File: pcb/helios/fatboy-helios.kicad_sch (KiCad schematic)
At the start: 76 parts, among them SW1 SW_Push, U1 Helios

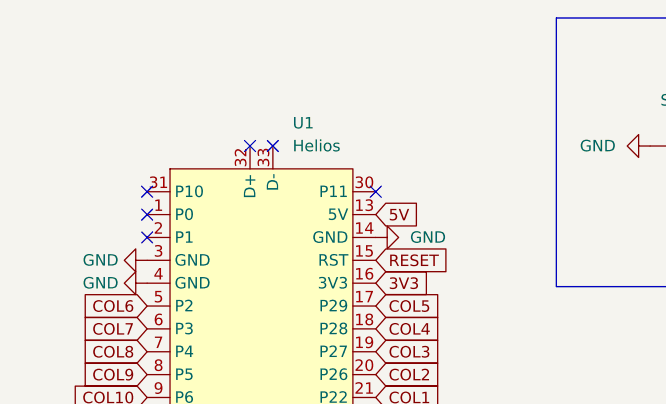
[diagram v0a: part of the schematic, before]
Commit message: helios: use `libs/marbastlib` for symbols and footprints
Instead of implicitly relying on the assumption that the `marbastlib`
(or any other library, really) will be present in development
environment, expliciltly rely on the respective submodule version
of the library
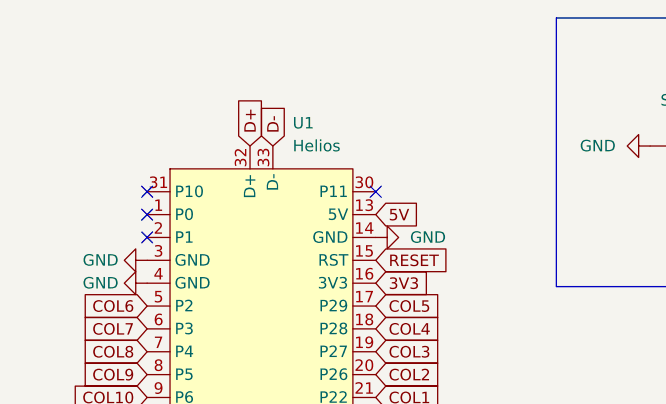
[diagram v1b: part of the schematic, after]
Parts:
- removed MX10, MX11, MX12, MX13, MX14, MX15, MX16, MX17, MX18, MX19, MX2, MX20, MX21, MX22, MX23, MX24, MX25, MX26, MX27, MX28, MX29, MX3, MX30, MX31, MX32, MX33, MX34, MX35, MX36, MX4, MX5, MX6, MX7, MX8, MX9: MX_SW_HS, PCM_marbastlib-mx:SW_MX_HS_CPG151101S11_1u, symbol PCM_marbastlib-mx:MX_SW_HS_CPG151101S11
- added MX10, MX11, MX12, MX13, MX14, MX15, MX16, MX17, MX18, MX19, MX2, MX20, MX21, MX22, MX23, MX24, MX25, MX26, MX27, MX28, MX29, MX3, MX30, MX31, MX32, MX33, MX34, MX35, MX36, MX4, MX5, MX6, MX7, MX8, MX9: MX_SW_HS, marbastlib-mx:SW_MX_HS_CPG151101S11_1u, symbol marbastlib-mx:MX_SW_HS_CPG151101S11
- LED1, LED2: symbol PCM_marbastlib-various:SK6812MINI-E -> marbastlib-various:SK6812MINI-E
- MX1: footprint PCM_marbastlib-mx:SW_MX_HS_CPG151101S11_1u -> marbastlib-mx:SW_MX_HS_CPG151101S11_1u; symbol PCM_marbastlib-mx:MX_SW_HS_CPG151101S11 -> marbastlib-mx:MX_SW_HS_CPG151101S11
- SW1: footprint PCM_marbastlib-various:SW_SKHLLCA010 -> marbastlib-various:SW_SKHLLCA010
- U1: symbol PCM_marbastlib-promicroish:Helios -> marbastlib-promicroish:Helios
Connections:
- net COL1: now also MX11.1, MX21.1
- net COL10: now also MX10.1, MX20.1, MX30.1
- net COL2: now also MX12.1, MX2.1, MX22.1
- net COL3: now also MX13.1, MX23.1, MX3.1, MX31.1
- net COL4: now also MX14.1, MX24.1, MX32.1, MX4.1
- net COL5: now also MX15.1, MX25.1, MX33.1, MX5.1
- net COL6: now also MX16.1, MX26.1, MX34.1, MX6.1
- net COL7: now also MX17.1, MX27.1, MX35.1, MX7.1
- net COL8: now also MX18.1, MX28.1, MX36.1, MX8.1
- net COL9: now also MX19.1, MX29.1, MX9.1
- net at D19.2 (A): now also MX19.2
- net at D4.2 (A): now also MX4.2
- net at D6.2 (A): now also MX6.2
- net at D17.2 (A): now also MX17.2
- net at D2.2 (A): now also MX2.2
- net at D15.2 (A): now also MX15.2
- net at D23.2 (A): now also MX23.2
- net at D11.2 (A): now also MX11.2
- net at D20.2 (A): now also MX20.2
- net at D3.2 (A): now also MX3.2
- net at D33.2 (A): now also MX33.2
- net D+: now reaches U1.32 (D+)
- net D-: now reaches U1.33 (D-)
- net at D16.2 (A): now also MX16.2
- net at D12.2 (A): now also MX12.2
- net at D8.2 (A): now also MX8.2
- net at D13.2 (A): now also MX13.2
- net at D30.2 (A): now also MX30.2
- net at D25.2 (A): now also MX25.2
- net at D27.2 (A): now also MX27.2
- net at D10.2 (A): now also MX10.2
- net at D21.2 (A): now also MX21.2
- net at D14.2 (A): now also MX14.2
- net at D28.2 (A): now also MX28.2
- net at D32.2 (A): now also MX32.2
- net at D34.2 (A): now also MX34.2
- net at D31.2 (A): now also MX31.2
- net at D36.2 (A): now also MX36.2
- net at D9.2 (A): now also MX9.2
- net at D24.2 (A): now also MX24.2
- net at D22.2 (A): now also MX22.2
- net at D35.2 (A): now also MX35.2
- net at D29.2 (A): now also MX29.2
- net at D18.2 (A): now also MX18.2
- net at D5.2 (A): now also MX5.2
- net at D7.2 (A): now also MX7.2
- net at D26.2 (A): now also MX26.2
- no-connect marks 14 -> 12
